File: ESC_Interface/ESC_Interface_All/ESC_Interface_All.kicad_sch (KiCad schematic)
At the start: 11 parts, among them J1 Conn_01x03_Pin, J2 B4PS-VH, J3 4P_Header, J4 B2PS-VH, J5 Conn_2Rows-09Pins, P1 DB25_Male, P2 DSUB15 Male, P3 DA15, P4 DSUB9 Male

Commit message: Add files via upload
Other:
- note added: "AGP 25 G-ME"
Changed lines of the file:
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@@
+    (effects (font (size 1.27 1.27)) (justify left bottom))
+  )
+  (text "AGP 25 G-ME" (at 53.34 96.52 0)
     (effects (font (size 1.27 1.27)) (justify left bottom))
   )

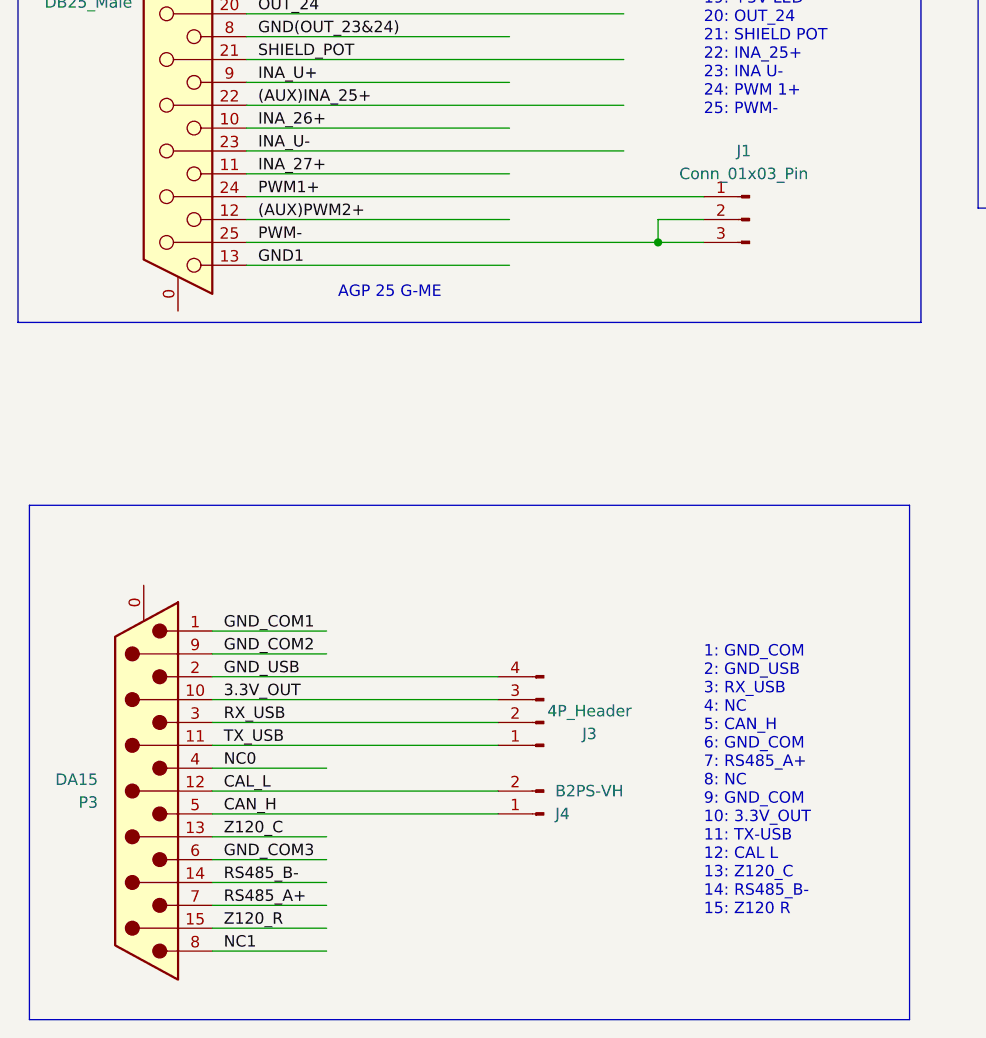
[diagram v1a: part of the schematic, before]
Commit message: Fixed P3 material error
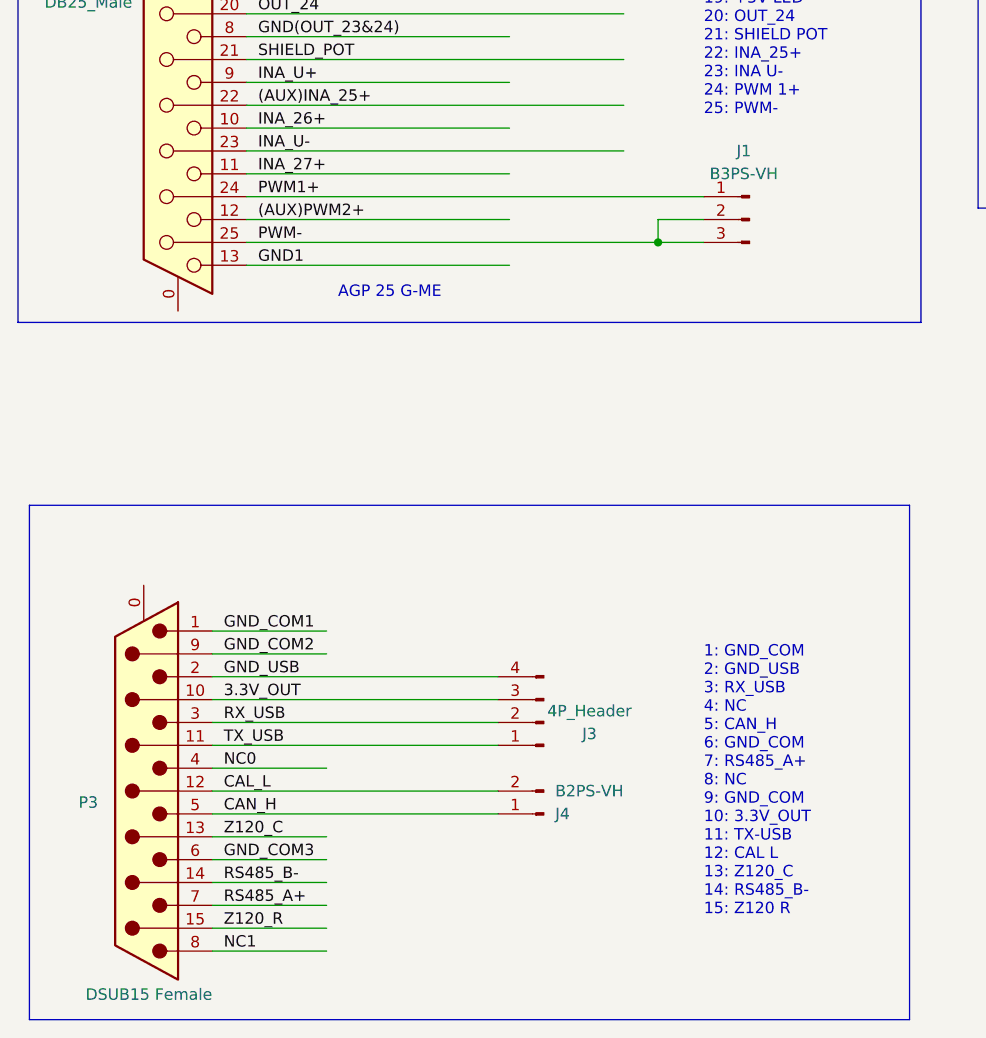
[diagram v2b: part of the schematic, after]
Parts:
- J1: value Conn_01x03_Pin -> B3PS-VH; Link (none) -> https://www.digikey.jp/en/products/detail/jst-sales-america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; MPN (none) -> B3PS-VH
- J2: Link (none) -> https://www.digikey.jp/en/products/detail/jst-sales-america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; MPN (none) -> B4PS-VH
- J4: Link (none) -> https://www.digikey.jp/en/products/detail/jst-sales-america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; MPN (none) -> B2PS-VH
- P3: value DA15 -> DSUB15 Female; Link (none) -> https://www.digikey.jp/en/products/detail/amphenol-cs-fci/D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; MPN (none) -> DA15P064HTXLF

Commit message: Add files via upload
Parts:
- renumbered P3 to P2, P2 to P3
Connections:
- net (GND_EXT): now also P2.8; no longer P3.1
- net +12V_EXT: now also P2.11 (P111); no longer P3.13 (P13)
- net 3.3V_OUT: now also P3.14 (P14); no longer P2.10 (P10)
- net CAL_L: now also P3.12 (P12); no longer P2.12 (P12)
- net CAN_H: now also P3.4; no longer P2.5
- net CONTACTOR+: now also P2.13 (P13); no longer P3.11 (P111)
- net CONTACTOR-: now also P2.14 (P14); no longer P3.10 (P10)
- net EMERG_IN+: now also P2.5; no longer P3.4
- net EMERG_IN-: now also P2.4; no longer P3.5
- net EMERG_U-: now also P2.15 (P15); no longer P3.9 (P9)
- net ENERG_U+: now also P2.12 (P12); no longer P3.12 (P12)
- net GND_COM1: now also P3.8; no longer P2.1
- net GND_COM2: now also P3.15 (P15); no longer P2.9 (P9)
- net GND_COM3: now also P3.3; no longer P2.6
- net GND_EXT: now also P2.3; no longer P3.6
- net GND_USB: now also P3.7; no longer P2.2
- net KEY+: now also P2.10 (P10); no longer P3.14 (P14)
- net KEY-: now also P2.2; no longer P3.7
- net LED+: now also P2.9 (P9); no longer P3.15 (P15)
- net LED-: now also P2.1; no longer P3.8
- net NC0: now also P3.5; no longer P2.4
- net NC1: now also P3.1; no longer P2.8
- net RELAY+: now also P2.6; no longer P3.3
- net RELAY-: now also P2.7; no longer P3.2
- net RS485_A+: now also P3.2; no longer P2.7
- net RS485_B-: now also P3.10 (P10); no longer P2.14 (P14)
- net RX_USB: now also P3.6; no longer P2.3
- net TX_USB: now also P3.13 (P13); no longer P2.11 (P111)
- net Z120_C: now also P3.11 (P111); no longer P2.13 (P13)
- net Z120_R: now also P3.9 (P9); no longer P2.15 (P15)
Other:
- moved on the sheet: P2, P3
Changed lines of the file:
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@@
 	(symbol
 		(lib_id "Connector:DA15_Plug_MountingHoles")
-		(at 31.75 151.13 180)
+		(at 144.78 50.8 180)
 		(unit 1)
 		(exclude_from_sim no)
@@
 		(on_board yes)
 		(dnp no)
-		(property "Reference" "P3"
-			(at 26.67 152.4 0)
+		(property "Reference" "P2"
+			(at 139.7 52.07 0)
 			(effects
 				(font
@@
 		)
 		(property "Value" "DSUB15 Female"
-			(at 39.37 173.736 0)
+			(at 152.4 73.406 0)
 			(effects
 				(font
@@
 		)
 		(property "Footprint" "Connector_Dsub:DSUB-15_Male_EdgeMount_P2.77mm_1"
-			(at 31.75 151.13 0)
+			(at 144.78 50.8 0)
 			(effects
 				(font
@@
 		)
 		(property "Datasheet" " https://www.amphenol-cs.com/media/wysiwyg/files/drawing/c-dsub-0064.pdf "
-			(at 31.75 151.13 0)
+			(at 144.78 50.8 0)
 			(effects
 				(font
@@
 		)
 		(property "Description" "15 Position D-Sub Plug, Male Pins Connector "
-			(at 31.75 151.13 0)
+			(at 144.78 50.8 0)
 			(effects
 				(font
@@
 		)
 		(property "MPN" "DA15P064HTXLF"
-			(at 31.75 151.13 0)
+			(at 144.78 50.8 0)
 			(effects
 				(font
@@
 		)
 		(property "Link" "https://www.digikey.jp/en/products/detail/amphenol-cs-fci/DA15P064HTXLF/1536743 "
-			(at 31.75 151.13 0)
+			(at 144.78 50.8 0)
 			(effects
 				(font
@@
 			(project "ESC_Interface_All"
 				(path "/bf8f5c90-8ff0-43e2-b961-b1dc2fdb4261"
-					(reference "P3")
+					(reference "P2")
 					(unit 1)
 				)
@@
 	(symbol
 		(lib_id "Connector:DA15_Plug_MountingHoles")
-		(at 144.78 50.8 0)
+		(at 31.75 151.13 0)
 		(mirror y)
 		(unit 1)
@@
 		(on_board yes)
 		(dnp no)
-		(property "Reference" "P2"
-			(at 139.7 49.53 0)
+		(property "Reference" "P3"
+			(at 26.67 149.86 0)
 			(effects
 				(font
@@
 		)
 		(property "Value" "DSUB15 Male"
-			(at 139.7 52.07 0)
+			(at 38.1 175.514 0)
 			(effects
 				(font
@@
 		)
 		(property "Footprint" "Connector_Dsub:DSUB-15_Male_EdgeMount_P2.77mm_1"
-			(at 144.78 50.8 0)
+			(at 31.75 151.13 0)
 			(effects
 				(font
@@
 		)
 		(property "Datasheet" "https://cdn.amphenol-cs.com/media/wysiwyg/files/documentation/datasheet/inputoutput/io_dsub_brochure.pdf"
-			(at 144.78 50.8 0)
+			(at 31.75 151.13 0)
 			(effects
 				(font
@@
 		)
 		(property "Description" "CONN D-SUB RCPT 15POS SLDR CUP"
-			(at 144.78 50.8 0)
+			(at 31.75 151.13 0)
 			(effects
 				(font
@@
 		)
 		(property "MPN" "DA15S065HTLF"
-			(at 144.78 50.8 0)
+			(at 31.75 151.13 0)
 			(effects
 				(font
@@
 		)
 		(property "Link" "https://www.digikey.jp/en/products/detail/amphenol-icc-fci/DA15S065HTLF/1540823"
-			(at 144.78 50.8 0)
+			(at 31.75 151.13 0)
 			(effects
 				(font
@@
 			(project "ESC_Interface_All"
 				(path "/bf8f5c90-8ff0-43e2-b961-b1dc2fdb4261"
-					(reference "P2")
+					(reference "P3")
 					(unit 1)
 				)
